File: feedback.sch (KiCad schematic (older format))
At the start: 48 parts, among them J10 CONN_01X03, J11 CONN_01X03, J6 MICROFIT-10, J7 CONN_01X02, J8 CONN_01X03, J9 CONN_01X03

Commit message: progress on V2 schematic
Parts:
- removed C14, C24: DNP, Capacitors_SMD:C_0603, symbol C_Small
- removed C32, C33, C34, C35, C36: 470pF, Capacitors_SMD:C_0603, symbol C_Small
- removed J10, J11, J8, J9: CONN_01X03, sictroller:Molex-SL-3POS-RA, symbol CONN_01X03
- removed J6: MICROFIT-10, Connectors_Molex:Connector_Microfit3_Header_02x05_Angled_43045-100x, symbol MICROFIT-10
- removed R14, R15: DNP, Resistors_SMD:R_0603, symbol R_Small
- removed R35: 1.8K, Resistors_SMD:R_0603, symbol R_Small
- removed R36: 3.3K, Resistors_SMD:R_0603, symbol R_Small
- removed R5: 2.2K, Resistors_SMD:R_0603, symbol R_Small
- added C? (x6): 0.1uF, Capacitors_SMD:C_0603, symbol C_Small
- added D?: D_Schottky_Small, symbol D_Schottky_Small
- added I? (x3): ACS770, symbol ACS770
- added J? (x5): RINGTERM, symbol CONN_01X01
- added J?: CONN_01X02, sictroller:Molex-SL-2POS-RA, symbol CONN_01X02
- added Q?: CSD17483F4, symbol Q_NMOS_GSD
- added R?: 2.7K, Resistors_SMD:R_0603, symbol R_Small
- added R? (x2): 10K, Resistors_SMD:R_0603, symbol R_Small
- added R?: 56K, Resistors_SMD:R_0603, symbol R_Small
- added R?: 100K, Resistors_SMD:R_0603, symbol R_Small
- added TH?: THERMISTOR, symbol THERMISTOR
- added U?: ADUM5241, symbol ADUM5241
- added U?: MAX6691, symbol MAX6691
- C20, C22, C23: value DNP -> 1nF
- R10, R13, R19, R22: value 1.8K 1% -> 3.6K 1%
- R11, R12, R17, R18, R20, R21, R8, R9: value 150K 1% 250V 0.5W -> 300K 1% 250V 0.5W
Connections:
- net labels added: +5VD, +5V_therm, BUS+, BUS-, CCS_NTC_1, CCS_NTC_2, GND_therm, TEMP_EN, TEMP_PWM, ~IFB_A
- net labels removed: HV+, HV-, IFB_A, IFB_BUS, MOTOR_TEMP, PWR_TEMP, PWR_TEMP_IN, VsL_A, VsL_B, VsL_C
- wire segments 80 -> 130
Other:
- note added: "Heatsink temperature"
- note added: "KTY81/210 temp sensor\n -10 C: 1.5k\n+150 C: 4.3k"
- note added: "Power stage PCB temperature"
- note removed: "KTY81/210 temp sensor\n -10 C: 1.5k => 2.97 V\n+150 C: 4.3k => 1.69 V"
- note removed: "Power stage temperature\n(will need some hacks)"
- moved on the sheet: C10, C11, C15, C16, C20, C22, C23, C28, C29, C30, C31, J7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

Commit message: more v2 progress
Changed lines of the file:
@@
 	2250 2000 2250 2050
 Wire Wire Line
-	2250 2250 2250 2350
-Wire Wire Line
-	2250 2350 2250 2400
+	2250 2250 2250 2400
 Wire Wire Line
 	2250 2600 2250 2650
 Wire Wire Line
-	2250 2400 2450 2400
-Wire Wire Line
-	2450 2400 2600 2400
-Wire Wire Line
-	2250 2600 2450 2600
-Wire Wire Line
-	2450 2600 2600 2600
+	2250 2400 2600 2400
+Wire Wire Line
+	2250 2600 2600 2600
 Wire Wire Line
 	2300 2350 2250 2350
@@
 	3150 2000 3150 2050
 Wire Wire Line
-	3150 2250 3150 2350
-Wire Wire Line
-	3150 2350 3150 2400
+	3150 2250 3150 2400
 Wire Wire Line
 	3150 2600 3150 2650
 Wire Wire Line
-	3150 2400 3350 2400
-Wire Wire Line
-	3350 2400 3500 2400
-Wire Wire Line
-	3150 2600 3350 2600
-Wire Wire Line
-	3350 2600 3500 2600
+	3150 2400 3500 2400
+Wire Wire Line
+	3150 2600 3500 2600
 Wire Wire Line
 	3200 2350 3150 2350
@@
 	4100 2000 4100 2050
 Wire Wire Line
-	4100 2250 4100 2350
-Wire Wire Line
-	4100 2350 4100 2400
+	4100 2250 4100 2400
 Wire Wire Line
 	4100 2600 4100 2650
 Wire Wire Line
-	4100 2400 4300 2400
-Wire Wire Line
-	4300 2400 4450 2400
-Wire Wire Line
-	4100 2600 4300 2600
-Wire Wire Line
-	4300 2600 4450 2600
+	4100 2400 4450 2400
+Wire Wire Line
+	4100 2600 4450 2600
 Wire Wire Line
 	4150 2350 4100 2350
@@
 	5050 2000 5050 2050
 Wire Wire Line
-	5050 2250 5050 2350
-Wire Wire Line
-	5050 2350 5050 2400
+	5050 2250 5050 2400
 Wire Wire Line
 	5050 2600 5050 2650
 Wire Wire Line
-	5050 2400 5250 2400
-Wire Wire Line
-	5250 2400 5400 2400
-Wire Wire Line
-	5050 2600 5250 2600
-Wire Wire Line
-	5250 2600 5400 2600
+	5050 2400 5400 2400
+Wire Wire Line
+	5050 2600 5400 2600
 Wire Wire Line
 	5100 2350 5050 2350
@@
 	5050 1100 5050 1800
 Wire Wire Line
-	9300 1850 9300 1950
-Wire Wire Line
-	9300 1950 9300 2000
+	9300 1850 9300 2000
 Wire Wire Line
 	9300 2200 9300 2250
@@
 Connection ~ 9300 1950
 Wire Wire Line
-	9300 3650 9300 3750
-Wire Wire Line
-	9300 3750 9300 3800
+	9300 3650 9300 3800
 Wire Wire Line
 	9300 4000 9300 4050
@@
 Connection ~ 9300 3750
 Wire Wire Line
-	9300 5450 9300 5550
-Wire Wire Line
-	9300 5550 9300 5600
+	9300 5450 9300 5600
 Wire Wire Line
 	9300 5800 9300 5850
@@
 	3250 5250 3200 5250
 Wire Wire Line
-	3250 4700 3250 5000
-Wire Wire Line
-	3250 5000 3250 5250
-Wire Wire Line
-	3250 5000 3650 5000
-Wire Wire Line
-	3650 5000 4050 5000
-Wire Wire Line
-	4050 4700 4050 5000
-Wire Wire Line
-	4050 5000 4050 5250
+	3250 4700 3250 5250
+Wire Wire Line
+	3250 5000 4050 5000
+Wire Wire Line
+	4050 4700 4050 5250
 Wire Wire Line
 	3200 5550 4050 5550
@@
 	2500 5850 2500 5650
 Wire Wire Line
-	3200 5350 3650 5350
-Wire Wire Line
-	3650 5350 3850 5350
-Wire Wire Line
-	3850 5350 4050 5350
+	3200 5350 4050 5350
 $Comp
 L D_Schottky_Small D?
@@
 $EndComp
 Wire Wire Line
-	5600 5900 5600 5700
-Wire Wire Line
-	5600 5700 5600 5650
+	5600 5650 5600 5900
 Wire Wire Line
 	5600 5700 5300 5700
@@
 	6300 6050 6300 5900
 Wire Wire Line
-	6300 5700 6300 5650
-Wire Wire Line
-	6300 5650 6300 5600
+	6300 5600 6300 5700
 Wire Wire Line
 	6400 5650 6300 5650

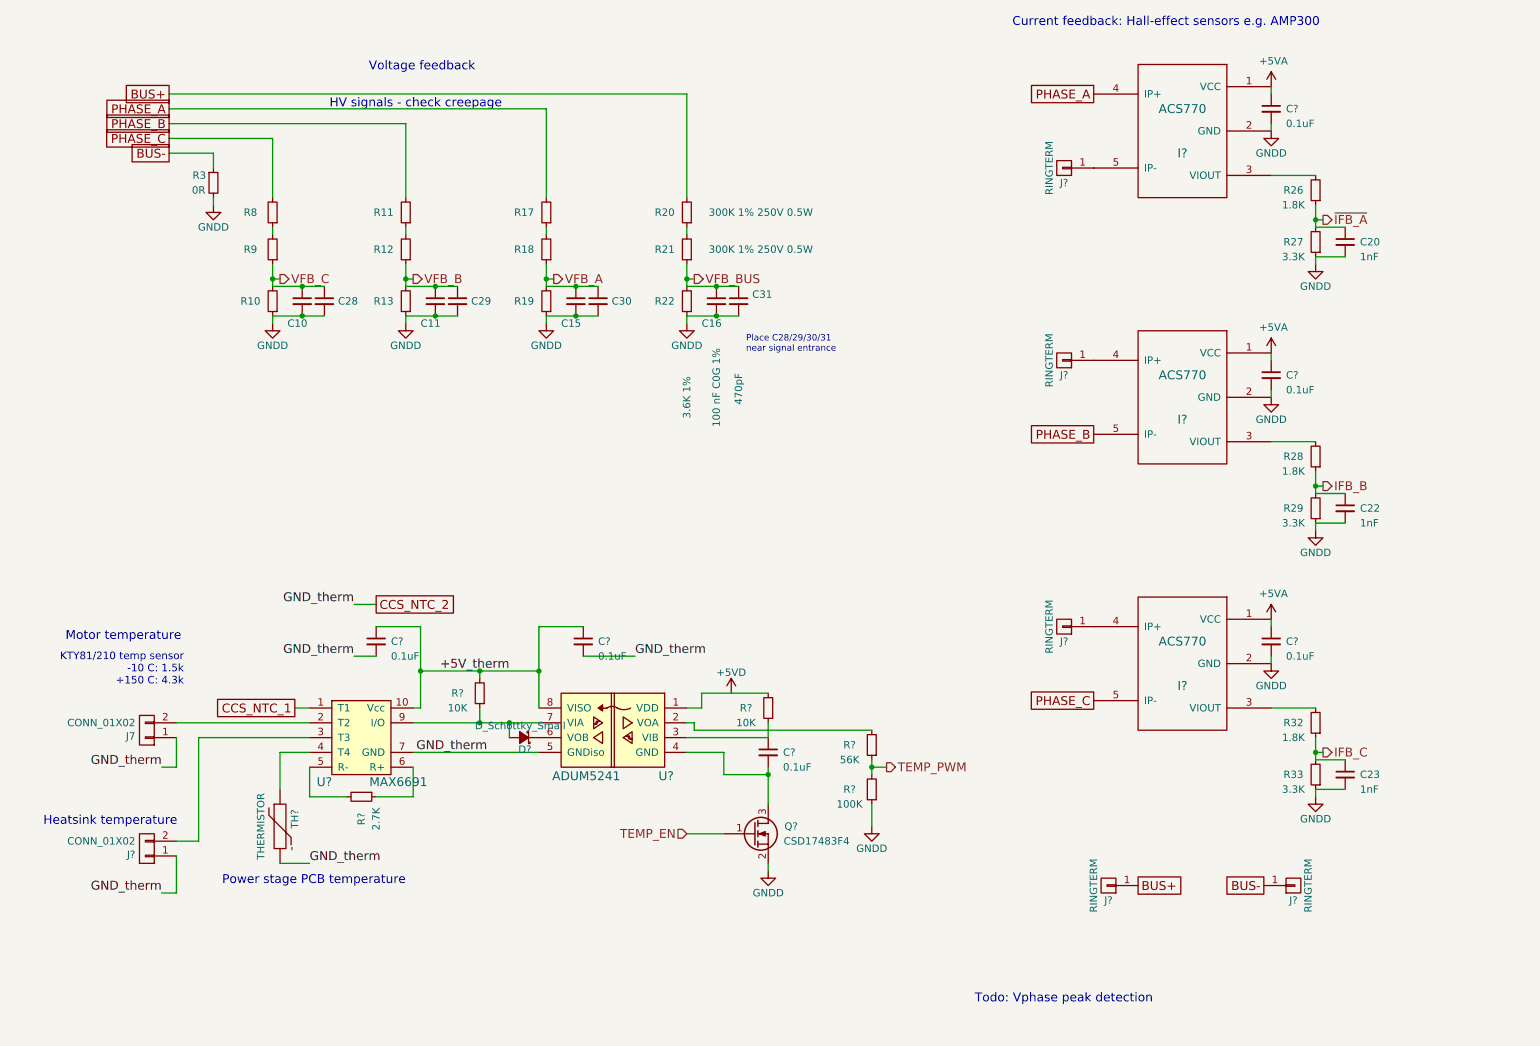
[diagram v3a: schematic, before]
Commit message: V2 schem complete, footprints not assigned
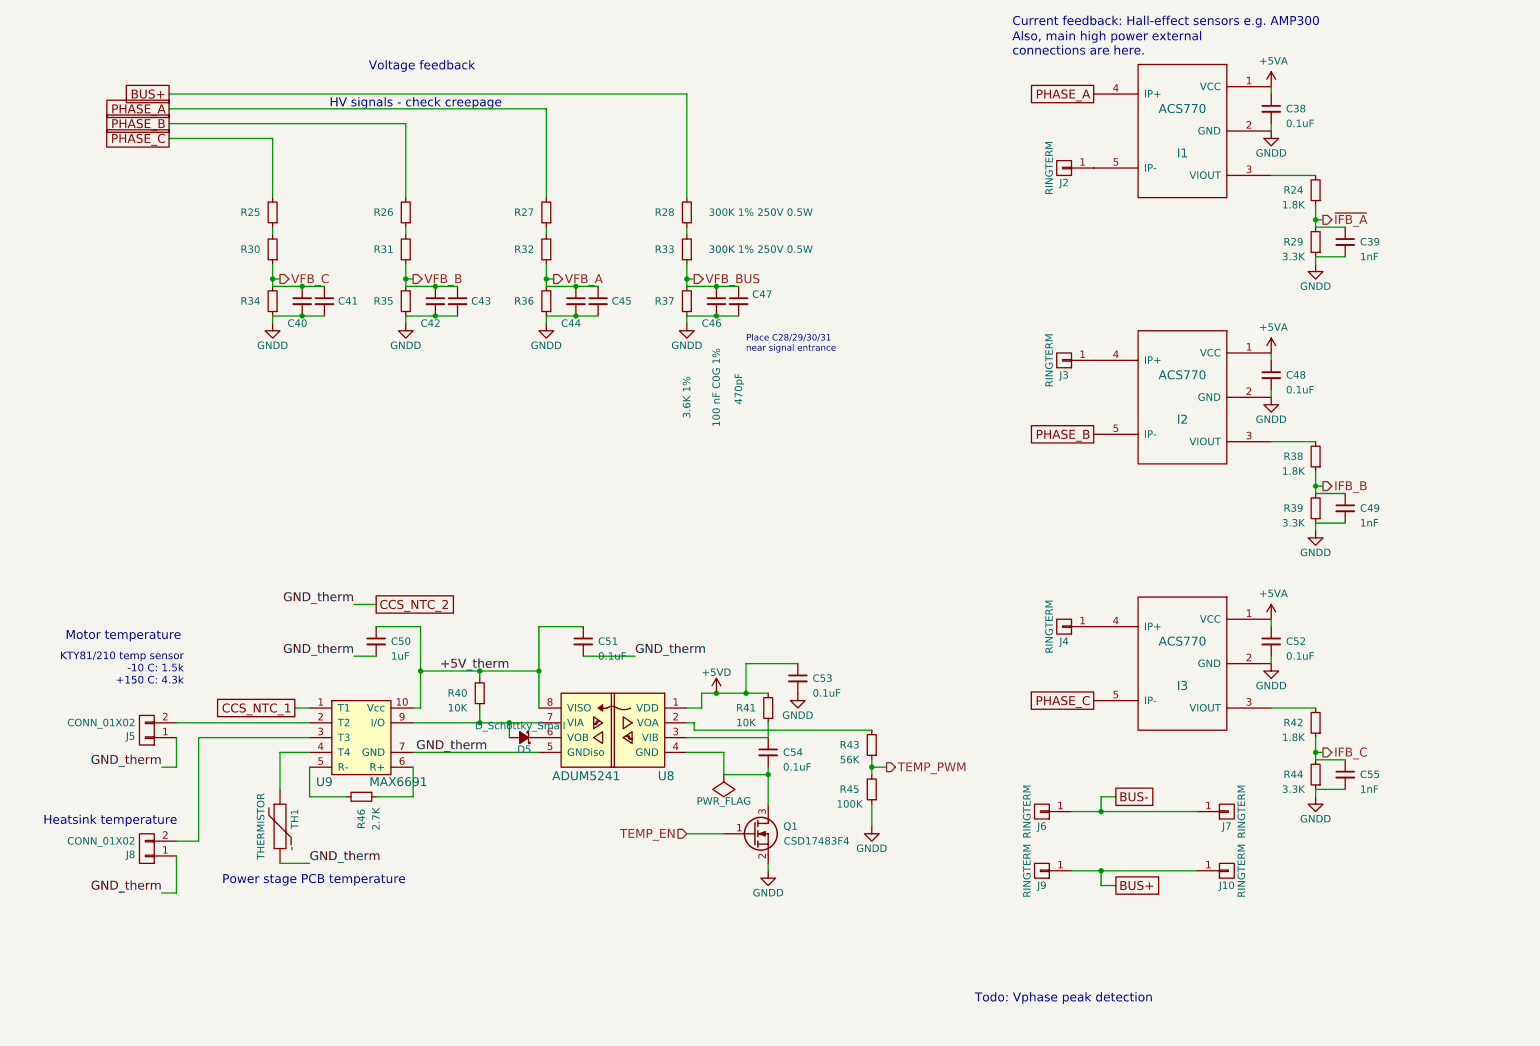
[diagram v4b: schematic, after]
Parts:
- removed R3: 0R, Resistors_SMD:R_0603, symbol R_Small
- added C53: 0.1uF, Capacitors_SMD:C_0603, symbol C_Small
- added J6, J7: RINGTERM, symbol CONN_01X01
- C50: renamed from C?; value 0.1uF -> 1uF
- gave numbers to parts that had none: 24
- renumbered C20 to C39, C10 to C40, C28 to C41, C11 to C42, C29 to C43, C15 to C44, C30 to C45, C16 to C46, C31 to C47, C22 to C49, C23 to C55, J7 to J5, R26 to R24, R8 to R25, R11 to R26, R17 to R27, R20 to R28, R27 to R29, R9 to R30, R12 to R31, R18 to R32, R21 to R33, R10 to R34, R13 to R35, R19 to R36, R22 to R37, R28 to R38, R29 to R39, R32 to R42, R33 to R44
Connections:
- net +5VD: now also R41.2, U8.1 (VDD), C53.1
- net BUS+: now also J10.1 (P1)
- net BUS-: now also J6.1 (P1), J7.1 (P1); no longer J10.1 (P1)
- net GNDD: now also C53.2
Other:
- note added: "Also, main high power external\nconnections are here."
- moved on the sheet: J10, J9

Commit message: Add TVS protection to signal I/O.  Reannotate. Assign some footprints.
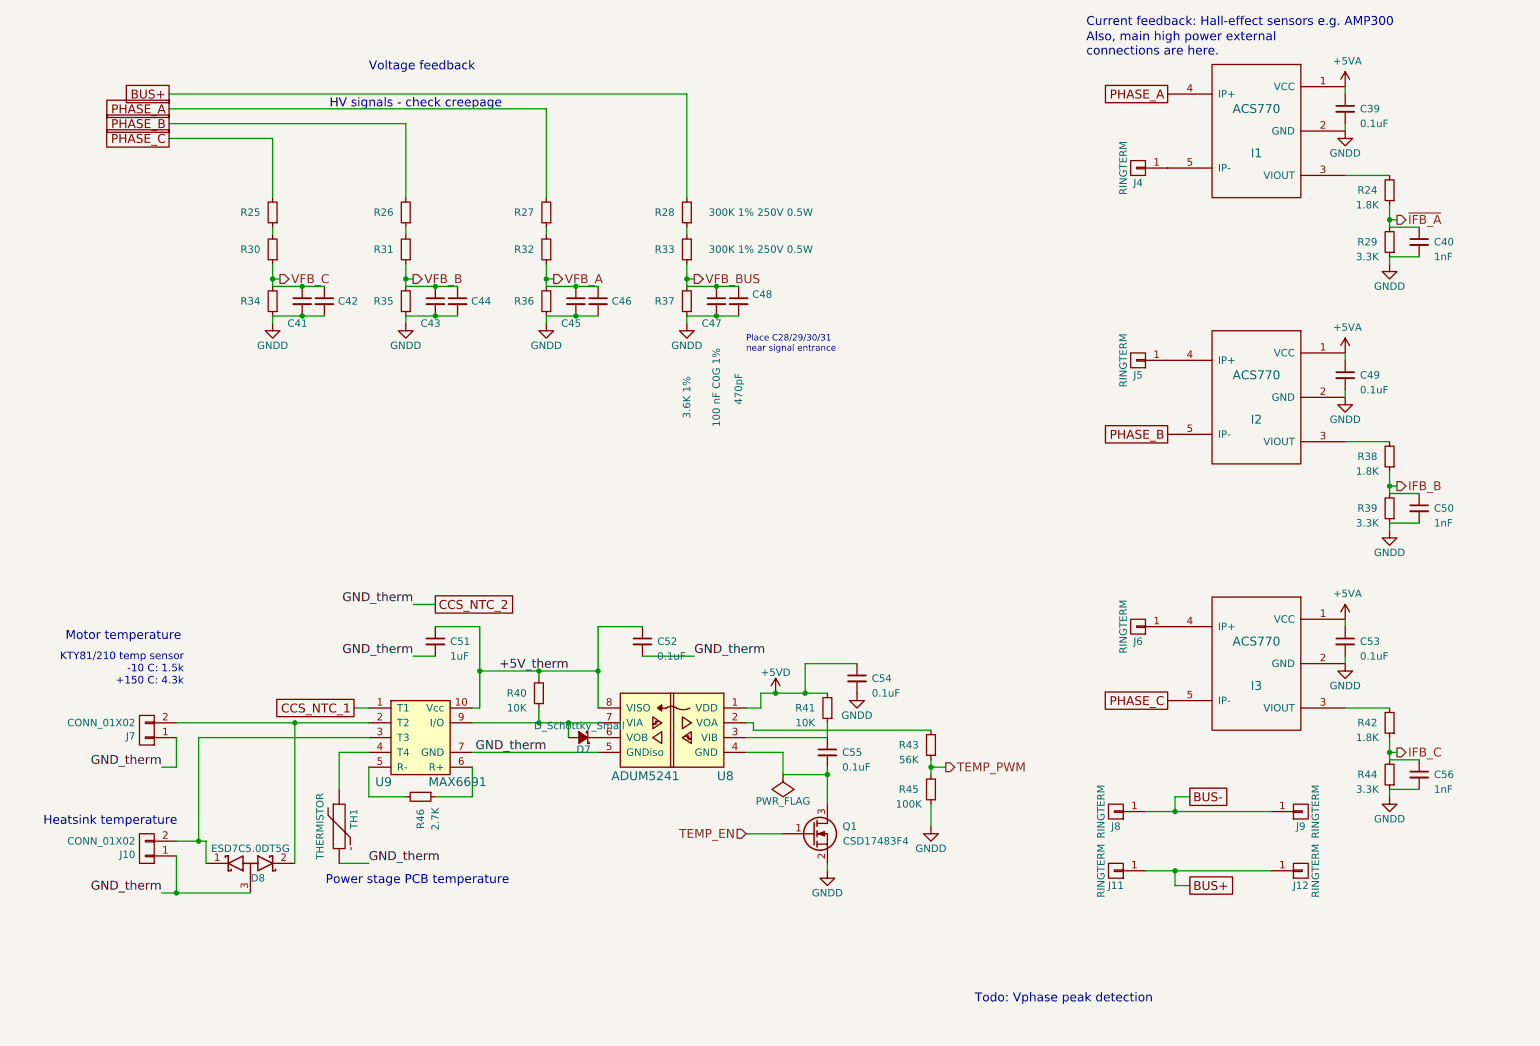
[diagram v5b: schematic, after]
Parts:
- added D8: ESD7C5.0DT5G, sictroller:SOT-723, symbol D_Schottky_x2_ACom_KKA
- renumbered C38 to C39, C39 to C40, C40 to C41, C41 to C42, C42 to C43, C43 to C44, C44 to C45, C45 to C46, C46 to C47, C47 to C48, C48 to C49, C49 to C50, C50 to C51, C51 to C52, C52 to C53, C53 to C54, C54 to C55, C55 to C56, D5 to D7, J8 to J10, J9 to J11, J10 to J12, J2 to J4, J3 to J5, J4 to J6, J5 to J7, J6 to J8, J7 to J9
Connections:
- net CCS_NTC_2: now also D8.3 (A)
- net at J7.2 (P2), U9.2 (T2): now also D8.2 (K)
- net at J10.2 (P2), U9.3 (T3): now also D8.1 (K)
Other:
- moved on the sheet: C39, C40, C49, C50, C51, C52, C53, C54, C55, C56, D7, I1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
